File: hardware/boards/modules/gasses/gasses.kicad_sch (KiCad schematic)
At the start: 26 parts, among them J1 Program Header, M1 MiCS-6814, U9 Buffer

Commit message: REFACTO relinked every kicad projects
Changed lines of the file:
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@@
 		(pin "1"
 		)
-		(pin "3"
+		(pin ""
 		)
 		(pin "2"

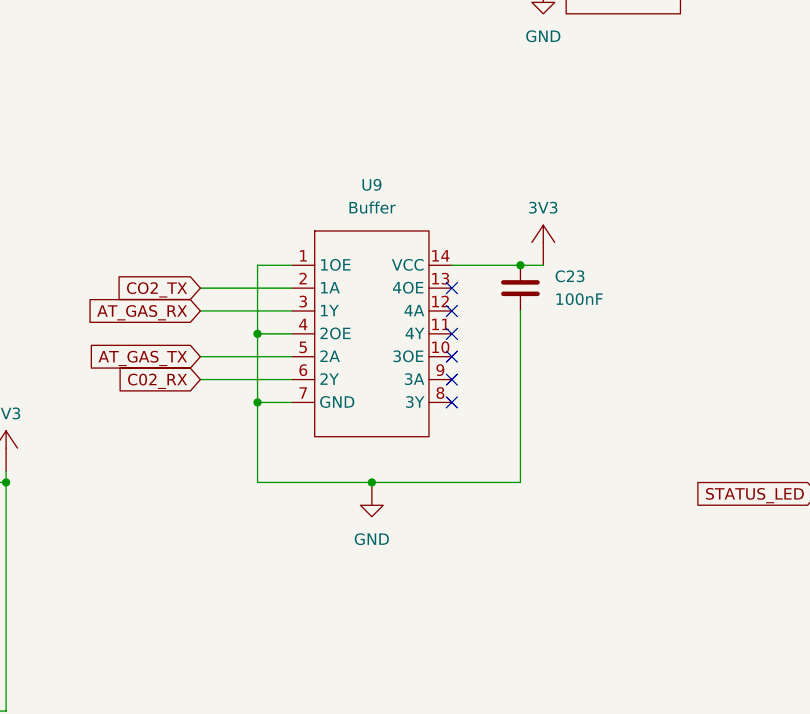
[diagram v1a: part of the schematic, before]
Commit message: redesigned gas module pcb
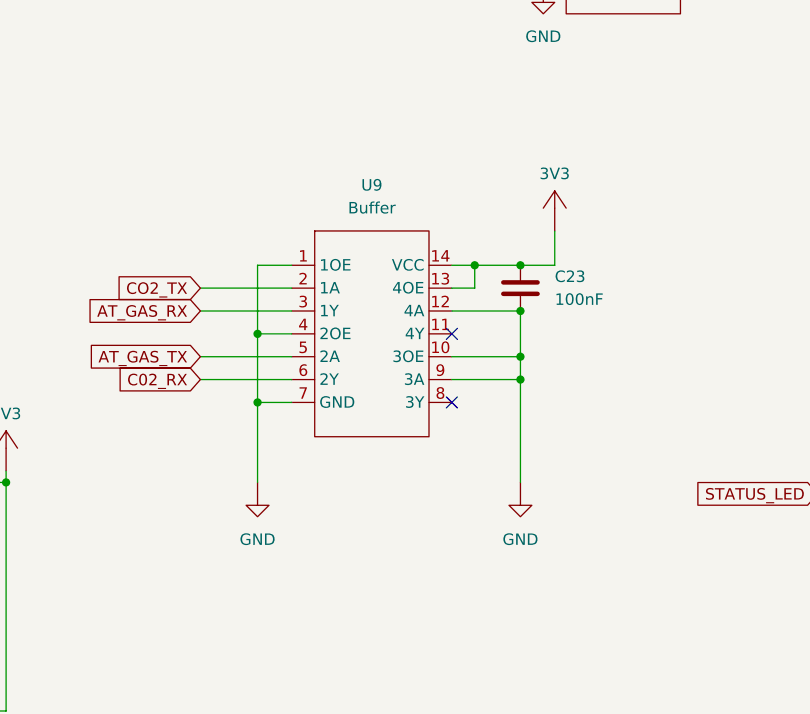
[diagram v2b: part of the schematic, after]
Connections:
- net 3V3: now also U9.13 (4OE)
- net GND: now also U9.10 (3OE), U9.12 (4A), U9.9 (3A)
- no-connect marks 13 -> 9
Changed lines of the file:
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@@
 	)
 	(junction
+		(at 210.82 129.54)
+		(diameter 0)
+		(color 0 0 0 0)
+	)
+	(junction
 		(at 181.61 132.08)
 		(diameter 0)
@@
 	)
 	(junction
-		(at 72.39 173.99)
+		(at 205.74 116.84)
 		(diameter 0)
 		(color 0 0 0 0)
 	)
 	(junction
-		(at 107.95 170.18)
+		(at 72.39 173.99)
 		(diameter 0)
 		(color 0 0 0 0)
 	)
 	(junction
-		(at 194.31 140.97)
+		(at 107.95 170.18)
 		(diameter 0)
 		(color 0 0 0 0)
@@
 	)
 	(junction
+		(at 210.82 127)
+		(diameter 0)
+		(color 0 0 0 0)
+	)
+	(junction
 		(at 59.69 173.99)
 		(diameter 0)
@@
 		(color 0 0 0 0)
 	)
-	(no_connect
-		(at 203.2 127)
-	)
-	(no_connect
-		(at 203.2 119.38)
-	)
-	(no_connect
-		(at 203.2 129.54)
+	(junction
+		(at 210.82 121.92)
+		(diameter 0)
+		(color 0 0 0 0)
 	)
 	(no_connect
@@
 	)
 	(no_connect
-		(at 203.2 121.92)
-	)
-	(no_connect
 		(at 203.2 124.46)
 	)
@@
 	(wire
 		(pts
+			(xy 210.82 127) (xy 210.82 129.54)
+		)
+		(stroke
+			(width 0)
+			(type default)
+		)
+	)
+	(wire
+		(pts
 			(xy 96.52 165.1) (xy 96.52 170.18)
 		)
@@
 	(wire
 		(pts
+			(xy 214.63 116.84) (xy 210.82 116.84)
+		)
+		(stroke
+			(width 0)
+			(type default)
+		)
+	)
+	(wire
+		(pts
 			(xy 77.47 138.43) (xy 80.01 138.43)
 		)
@@
 	(wire
 		(pts
-			(xy 181.61 140.97) (xy 194.31 140.97)
+			(xy 59.69 165.1) (xy 72.39 165.1)
 		)
 		(stroke
@@
 	(wire
 		(pts
-			(xy 59.69 165.1) (xy 72.39 165.1)
+			(xy 77.47 138.43) (xy 77.47 144.78)
 		)
 		(stroke
@@
 	(wire
 		(pts
-			(xy 77.47 138.43) (xy 77.47 144.78)
+			(xy 69.85 138.43) (xy 77.47 138.43)
 		)
 		(stroke
@@
 	(wire
 		(pts
-			(xy 69.85 138.43) (xy 77.47 138.43)
+			(xy 181.61 132.08) (xy 181.61 140.97)
 		)
 		(stroke
@@
 	(wire
 		(pts
-			(xy 181.61 132.08) (xy 181.61 140.97)
+			(xy 104.14 118.11) (xy 104.14 125.73)
 		)
 		(stroke
@@
 	(wire
 		(pts
-			(xy 104.14 118.11) (xy 104.14 125.73)
+			(xy 205.74 119.38) (xy 205.74 116.84)
 		)
 		(stroke
@@
 	(wire
 		(pts
+			(xy 210.82 129.54) (xy 210.82 140.97)
+		)
+		(stroke
+			(width 0)
+			(type default)
+		)
+	)
+	(wire
+		(pts
 			(xy 201.93 71.12) (xy 201.93 60.96)
 		)
@@
 	(wire
 		(pts
+			(xy 203.2 119.38) (xy 205.74 119.38)
+		)
+		(stroke
+			(width 0)
+			(type default)
+		)
+	)
+	(wire
+		(pts
 			(xy 49.53 62.23) (xy 53.34 62.23)
 		)
@@
 	(wire
 		(pts
-			(xy 180.34 44.45) (xy 180.34 38.1)
+			(xy 205.74 116.84) (xy 210.82 116.84)
 		)
 		(stroke
@@
 	(wire
 		(pts
-			(xy 210.82 116.84) (xy 213.36 116.84)
+			(xy 180.34 44.45) (xy 180.34 38.1)
 		)
 		(stroke
@@
 	(wire
 		(pts
+			(xy 203.2 121.92) (xy 210.82 121.92)
+		)
+		(stroke
+			(width 0)
+			(type default)
+		)
+	)
+	(wire
+		(pts
 			(xy 49.53 73.66) (xy 77.47 73.66)
 		)
@@
 	(wire
 		(pts
-			(xy 203.2 116.84) (xy 210.82 116.84)
+			(xy 203.2 116.84) (xy 205.74 116.84)
 		)
 		(stroke
@@
 	(wire
 		(pts
-			(xy 210.82 140.97) (xy 194.31 140.97)
+			(xy 152.4 58.42) (xy 148.59 58.42)
 		)
 		(stroke
@@
 	(wire
 		(pts
-			(xy 152.4 58.42) (xy 148.59 58.42)
+			(xy 104.14 114.3) (xy 96.52 114.3)
 		)
 		(stroke
@@
 	(wire
 		(pts
-			(xy 104.14 114.3) (xy 96.52 114.3)
+			(xy 234.95 71.12) (xy 231.14 71.12)
 		)
 		(stroke
@@
 	(wire
 		(pts
-			(xy 234.95 71.12) (xy 231.14 71.12)
+			(xy 177.8 41.91) (xy 177.8 46.99)
 		)
 		(stroke
@@
 	(wire
 		(pts
-			(xy 177.8 41.91) (xy 177.8 46.99)
+			(xy 49.53 66.04) (xy 60.96 66.04)
 		)
 		(stroke
@@
 	(wire
 		(pts
-			(xy 49.53 66.04) (xy 60.96 66.04)
+			(xy 153.67 140.97) (xy 153.67 139.7)
 		)
 		(stroke
@@
 	(wire
 		(pts
-			(xy 153.67 140.97) (xy 153.67 139.7)
+			(xy 91.44 138.43) (xy 87.63 138.43)
 		)
 		(stroke
@@
 	(wire
 		(pts
-			(xy 210.82 121.92) (xy 210.82 140.97)
+			(xy 99.06 156.21) (xy 95.25 156.21)
 		)
 		(stroke
@@
 	(wire
 		(pts
-			(xy 91.44 138.43) (xy 87.63 138.43)
+			(xy 95.25 147.32) (xy 95.25 156.21)
 		)
 		(stroke
@@
 	(wire
 		(pts
-			(xy 99.06 156.21) (xy 95.25 156.21)
+			(xy 96.52 170.18) (xy 96.52 186.69)
 		)
 		(stroke
@@
 	(wire
 		(pts
-			(xy 95.25 147.32) (xy 95.25 156.21)
+			(xy 210.82 121.92) (xy 210.82 127)
 		)
 		(stroke
@@
 	(wire
 		(pts
-			(xy 96.52 170.18) (xy 96.52 186.69)
+			(xy 203.2 129.54) (xy 210.82 129.54)
 		)
 		(stroke
@@
 	(wire
 		(pts
+			(xy 214.63 113.03) (xy 214.63 116.84)
+		)
+		(stroke
+			(width 0)
+			(type default)
+		)
+	)
+	(wire
+		(pts
+			(xy 203.2 127) (xy 210.82 127)
+		)
+		(stroke
+			(width 0)
+			(type default)
+		)
+	)
+	(wire
+		(pts
 			(xy 175.26 127) (xy 185.42 127)
 		)
@@
 	(symbol
 		(lib_id "pwr:GND")
-		(at 194.31 143.51 0)
+		(at 181.61 143.51 0)
 		(unit 1)
 		(exclude_from_sim no)
@@
 		(fields_autoplaced yes)
 		(property "Reference" "#GND012"
-			(at 194.31 130.51 0)
+			(at 181.61 130.51 0)
 			(effects
 				(font
@@
 		)
 		(property "Value" "GND"
-			(at 194.31 147.32 0)
+			(at 181.61 147.32 0)
 			(effects
 				(font
@@
 		)
 		(property "Footprint" ""
-			(at 194.31 143.51 0)
+			(at 181.61 143.51 0)
 			(effects
 				(font
@@
 		)
 		(property "Datasheet" ""
-			(at 194.31 143.51 0)
+			(at 181.61 143.51 0)
 			(effects
 				(font
@@
 		)
 		(property "Description" "Ground"
-			(at 194.31 148.01 0)
+			(at 181.61 148.01 0)
 			(effects
 				(font
@@
 	(symbol
 		(lib_id "pwr:GND")
+		(at 210.82 143.51 0)
+		(unit 1)
+		(exclude_from_sim no)
+		(in_bom no)
+		(on_board no)
+		(dnp no)
+		(fields_autoplaced yes)
+		(property "Reference" "#GND06"
+			(at 210.82 130.51 0)
+			(effects
+				(font
+					(size 1.27 1.27)
+				)
+				(hide yes)
+			)
+		)
+		(property "Value" "GND"
+			(at 210.82 147.32 0)
+			(effects
+				(font
+					(size 1.27 1.27)
+				)
+			)
+		)
+		(property "Footprint" ""
+			(at 210.82 143.51 0)
+			(effects
+				(font
+					(size 1.27 1.27)
+				)
+				(hide yes)
+			)
+		)
+		(property "Datasheet" ""
+			(at 210.82 143.51 0)
+			(effects
+				(font
+					(size 1.27 1.27)
+				)
+				(hide yes)
+			)
+		)
+		(property "Description" "Ground"
+			(at 210.82 148.01 0)
+			(effects
+				(font
+					(size 1.27 1.27)
+				)
+				(hide yes)
+			)
+		)
+		(pin "1"
+		)
+		(instances
+			(project ""
+				(path "/bd8bb99f-1696-40e4-a829-79b3479834af"
+					(reference "#GND06")
+					(unit 1)
+				)
+			)
+		)
+	)
+	(symbol
+		(lib_id "pwr:GND")
 		(at 111.76 120.65 0)
 		(unit 1)
@@
 	(symbol
 		(lib_id "pwr:+3.3V")
-		(at 213.36 114.3 0)
+		(at 214.63 110.49 0)
 		(unit 1)
 		(exclude_from_sim no)
@@
 		(fields_autoplaced yes)
 		(property "Reference" "#3V019"
-			(at 213.36 109.3 0)
+			(at 214.63 105.49 0)
 			(effects
 				(font
@@
 		)
 		(property "Value" "3V3"
-			(at 213.36 110.49 0)
+			(at 214.63 106.68 0)
 			(effects
 				(font
@@
 		)
 		(property "Footprint" ""
-			(at 213.36 114.3 0)
+			(at 214.63 110.49 0)
 			(effects
 				(font
@@
 		)
 		(property "Datasheet" ""
-			(at 213.36 114.3 0)
+			(at 214.63 110.49 0)
 			(effects
 				(font
@@
 		)
 		(property "Description" "+3.3V"
-			(at 213.36 127.3 0)
+			(at 214.63 123.49 0)
 			(effects
 				(font

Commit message: updated sensor module schematics
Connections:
- net C02_RX renamed CO2_RX
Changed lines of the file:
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@@
 		)
 	)
-	(global_label "C02_RX"
+	(global_label "CO2_RX"
 		(shape input)
 		(at 175.26 129.54 180)
@@
 		)
 		(property "Intersheetrefs" "${INTERSHEET_REFS}"
-			(at 165.1387 129.54 0)
+			(at 165.0177 129.54 0)
 			(effects
 				(font
@@
 		)
 	)
-	(global_label "C02_RX"
+	(global_label "CO2_RX"
 		(shape input)
 		(at 76.2 113.03 180)
@@
 		)
 		(property "Intersheetrefs" "${INTERSHEET_REFS}"
-			(at 66.0787 113.03 0)
+			(at 65.9577 113.03 0)
 			(effects
 				(font
@@
 		)
 		(instances
-			(project "air_sensor"
+			(project "gasses"
 				(path "/bd8bb99f-1696-40e4-a829-79b3479834af"
 					(reference "C12")
@@
 		)
 		(instances
-			(project "air_sensor"
+			(project "gasses"
 				(path "/bd8bb99f-1696-40e4-a829-79b3479834af"
 					(reference "#GND01")
@@
 		)
 		(instances
-			(project ""
+			(project "gasses"
 				(path "/bd8bb99f-1696-40e4-a829-79b3479834af"
 					(reference "#FLAG01")
@@
 		)
 		(instances
-			(project "air_sensor"
+			(project "gasses"
 				(path "/bd8bb99f-1696-40e4-a829-79b3479834af"
 					(reference "R1")
@@
 		)
 		(instances
-			(project "air_sensor"
+			(project "gasses"
 				(path "/bd8bb99f-1696-40e4-a829-79b3479834af"
 					(reference "R3")
@@
 		)
 		(instances
-			(project "air_sensor"
+			(project "gasses"
 				(path "/bd8bb99f-1696-40e4-a829-79b3479834af"
 					(reference "#GND012")
@@
 		)
 		(instances
-			(project "air_sensor"
+			(project "gasses"
 				(path "/bd8bb99f-1696-40e4-a829-79b3479834af"
 					(reference "C23")
@@
 		)
 		(instances
-			(project "air_sensor"
+			(project "gasses"
 				(path "/bd8bb99f-1696-40e4-a829-79b3479834af"
 					(reference "#GND029")
@@
 		)
 		(instances
-			(project "air_sensor"
+			(project "gasses"
 				(path "/bd8bb99f-1696-40e4-a829-79b3479834af"
 					(reference "#GND025")
@@
 		)
 		(instances
-			(project "air_sensor"
+			(project "gasses"
 				(path "/bd8bb99f-1696-40e4-a829-79b3479834af"
 					(reference "C15")
@@
 		)
 		(instances
-			(project "air_sensor"
+			(project "gasses"
 				(path "/bd8bb99f-1696-40e4-a829-79b3479834af"
 					(reference "#GND028")
@@
 		)
 		(instances
-			(project "air_sensor"
+			(project "gasses"
 				(path "/bd8bb99f-1696-40e4-a829-79b3479834af"
 					(reference "#5V012")
@@
 		)
 		(instances
-			(project "air_sensor"
+			(project "gasses"
 				(path "/bd8bb99f-1696-40e4-a829-79b3479834af"
 					(reference "#GND02")
@@
 		)
 		(instances
-			(project ""
+			(project "gasses"
 				(path "/bd8bb99f-1696-40e4-a829-79b3479834af"
 					(reference "#GND06")
@@
 		)
 		(instances
-			(project "air_sensor"
+			(project "gasses"
 				(path "/bd8bb99f-1696-40e4-a829-79b3479834af"
 					(reference "#GND041")
@@
 		)
 		(instances
-			(project "air_sensor"
+			(project "gasses"
 				(path "/bd8bb99f-1696-40e4-a829-79b3479834af"
 					(reference "C18")
@@
 		)
 		(instances
-			(project "air_sensor"
+			(project "gasses"
 				(path "/bd8bb99f-1696-40e4-a829-79b3479834af"
 					(reference "C32")
@@
 		)
 		(instances
-			(project "air_sensor"
+			(project "gasses"
 				(path "/bd8bb99f-1696-40e4-a829-79b3479834af"
 					(reference "U6")
@@
 		)
 		(instances
-			(project ""
+			(project "gasses"
 				(path "/bd8bb99f-1696-40e4-a829-79b3479834af"
 					(reference "R6")
@@
 		)
 		(instances
-			(project "air_sensor"
+			(project "gasses"
 				(path "/bd8bb99f-1696-40e4-a829-79b3479834af"
 					(reference "R11")
@@
 		)
 		(instances
-			(project "air_sensor"
+			(project "gasses"
 				(path "/bd8bb99f-1696-40e4-a829-79b3479834af"
 					(reference "#FLAG03")
@@
 		)
 		(instances
-			(project "air_sensor"
+			(project "gasses"
 				(path "/bd8bb99f-1696-40e4-a829-79b3479834af"
 					(reference "M1")
@@
 		)
 		(instances
-			(project "air_sensor"
+			(project "gasses"
 				(path "/bd8bb99f-1696-40e4-a829-79b3479834af"
 					(reference "#3V020")
@@
 		)
 		(instances
-			(project "air_sensor"
+			(project "gasses"
 				(path "/bd8bb99f-1696-40e4-a829-79b3479834af"
 					(reference "#3V016")
@@
 		)
 		(instances
-			(project "air_sensor"
+			(project "gasses"
 				(path "/bd8bb99f-1696-40e4-a829-79b3479834af"
 					(reference "A1")
@@
 		)
 		(instances
-			(project "air_sensor"
+			(project "gasses"
 				(path "/bd8bb99f-1696-40e4-a829-79b3479834af"
 					(reference "#5V011")
@@
 		)
 		(instances
-			(project "air_sensor"
+			(project "gasses"
 				(path "/bd8bb99f-1696-40e4-a829-79b3479834af"
 					(reference "G2")
@@
 		)
 		(instances
-			(project "air_sensor"
+			(project "gasses"
 				(path "/bd8bb99f-1696-40e4-a829-79b3479834af"
 					(reference "R5")
@@
 		)
 		(instances
-			(project ""
+			(project "gasses"
 				(path "/bd8bb99f-1696-40e4-a829-79b3479834af"
 					(reference "#GND05")
@@
 		)
 		(instances
-			(project "air_sensor"
+			(project "gasses"
 				(path "/bd8bb99f-1696-40e4-a829-79b3479834af"
 					(reference "R2")
@@
 		)
 		(instances
-			(project "air_sensor"
+			(project "gasses"
 				(path "/bd8bb99f-1696-40e4-a829-79b3479834af"
 					(reference "#FLAG02")
@@
 		)
 		(instances
-			(project "air_sensor"
+			(project "gasses"
 				(path "/bd8bb99f-1696-40e4-a829-79b3479834af"
 					(reference "#5V015")
@@
 		)
 		(instances
-			(project "air_sensor"
+			(project "gasses"
 				(path "/bd8bb99f-1696-40e4-a829-79b3479834af"
 					(reference "R12")
@@
 		)
 		(instances
-			(project "air_sensor"
+			(project "gasses"
 				(path "/bd8bb99f-1696-40e4-a829-79b3479834af"
 					(reference "#GND04")
@@
 		)
 		(instances
-			(project "air_sensor"
+			(project "gasses"
 				(path "/bd8bb99f-1696-40e4-a829-79b3479834af"
 					(reference "J1")
@@
 		)
 		(instances
-			(project ""
+			(project "gasses"
 				(path "/bd8bb99f-1696-40e4-a829-79b3479834af"
 					(reference "D1")
@@
 		)
 		(instances
-			(project "air_sensor"
+			(project "gasses"
 				(path "/bd8bb99f-1696-40e4-a829-79b3479834af"
 					(reference "R10")
@@
 		)
 		(instances
-			(project "air_sensor"
+			(project "gasses"
 				(path "/bd8bb99f-1696-40e4-a829-79b3479834af"
 					(reference "#FLAG06")
@@
 		)
 		(instances
-			(project "air_sensor"
+			(project "gasses"
 				(path "/bd8bb99f-1696-40e4-a829-79b3479834af"
 					(reference "S5")
@@
 		)
 		(instances
-			(project "air_sensor"
+			(project "gasses"
 				(path "/bd8bb99f-1696-40e4-a829-79b3479834af"
 					(reference "#3V017")
@@
 		)
 		(instances
-			(project "air_sensor"
+			(project "gasses"
 				(path "/bd8bb99f-1696-40e4-a829-79b3479834af"
 					(reference "#3V019")
@@
 		)
 		(instances
-			(project "air_sensor"
+			(project "gasses"
 				(path "/bd8bb99f-1696-40e4-a829-79b3479834af"
 					(reference "U9")
@@
 		)
 		(instances
-			(project "air_sensor"
+			(project "gasses"
 				(path "/bd8bb99f-1696-40e4-a829-79b3479834af"
 					(reference "C16")
@@
 		)
 		(instances
-			(project "air_sensor"
+			(project "gasses"
 				(path "/bd8bb99f-1696-40e4-a829-79b3479834af"
 					(reference "#GND030")
@@
 		)
 		(instances
-			(project "air_sensor"
+			(project "gasses"
 				(path "/bd8bb99f-1696-40e4-a829-79b3479834af"
 					(reference "R4")
@@
 		)
 		(instances
-			(project "air_sensor"
+			(project "gasses"
 				(path "/bd8bb99f-1696-40e4-a829-79b3479834af"
 					(reference "#5V014")
@@
 		)
 		(instances
-			(project "air_sensor"
+			(project "gasses"
 				(path "/bd8bb99f-1696-40e4-a829-79b3479834af"
 					(reference "#5V013")
@@
 		(pin "1"
 		)
-		(pin ""
+		(pin "3"
 		)
 		(pin "2"
 		)
 		(instances
-			(project "air_sensor"
+			(project "gasses"
 				(path "/bd8bb99f-1696-40e4-a829-79b3479834af"
 					(reference "O1")
@@
 		)
 		(instances
-			(project "air_sensor"
+			(project "gasses"
 				(path "/bd8bb99f-1696-40e4-a829-79b3479834af"
 					(reference "#GND03")
@@
 		)
 		(instances
-			(project "air_sensor"
+			(project "gasses"
 				(path "/bd8bb99f-1696-40e4-a829-79b3479834af"
 					(reference "C13")
@@
 		)
 		(instances
-			(project "air_sensor"
+			(project "gasses"
 				(path "/bd8bb99f-1696-40e4-a829-79b3479834af"
 					(reference "#GND036")
@@
 		)
 		(instances
-			(project "air_sensor"
+			(project "gasses"
 				(path "/bd8bb99f-1696-40e4-a829-79b3479834af"
 					(reference "C14")
@@
 		)
 		(instances
-			(project "air_sensor"
+			(project "gasses"
 				(path "/bd8bb99f-1696-40e4-a829-79b3479834af"
 					(reference "#3V018")
@@
 		)
 		(instances
-			(project "air_sensor"
+			(project "gasses"
 				(path "/bd8bb99f-1696-40e4-a829-79b3479834af"
 					(reference "#FLAG05")
@@
 		)
 		(instances
-			(project "air_sensor"
+			(project "gasses"
 				(path "/bd8bb99f-1696-40e4-a829-79b3479834af"
 					(reference "#FLAG07")
@@
 		)
 		(instances
-			(project "air_sensor"
+			(project "gasses"
 				(path "/bd8bb99f-1696-40e4-a829-79b3479834af"
 					(reference "#GND042")
